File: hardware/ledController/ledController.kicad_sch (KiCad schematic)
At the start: 5 parts, among them IC1 PIC16F1769-I_ML, J1 Conn_01x06

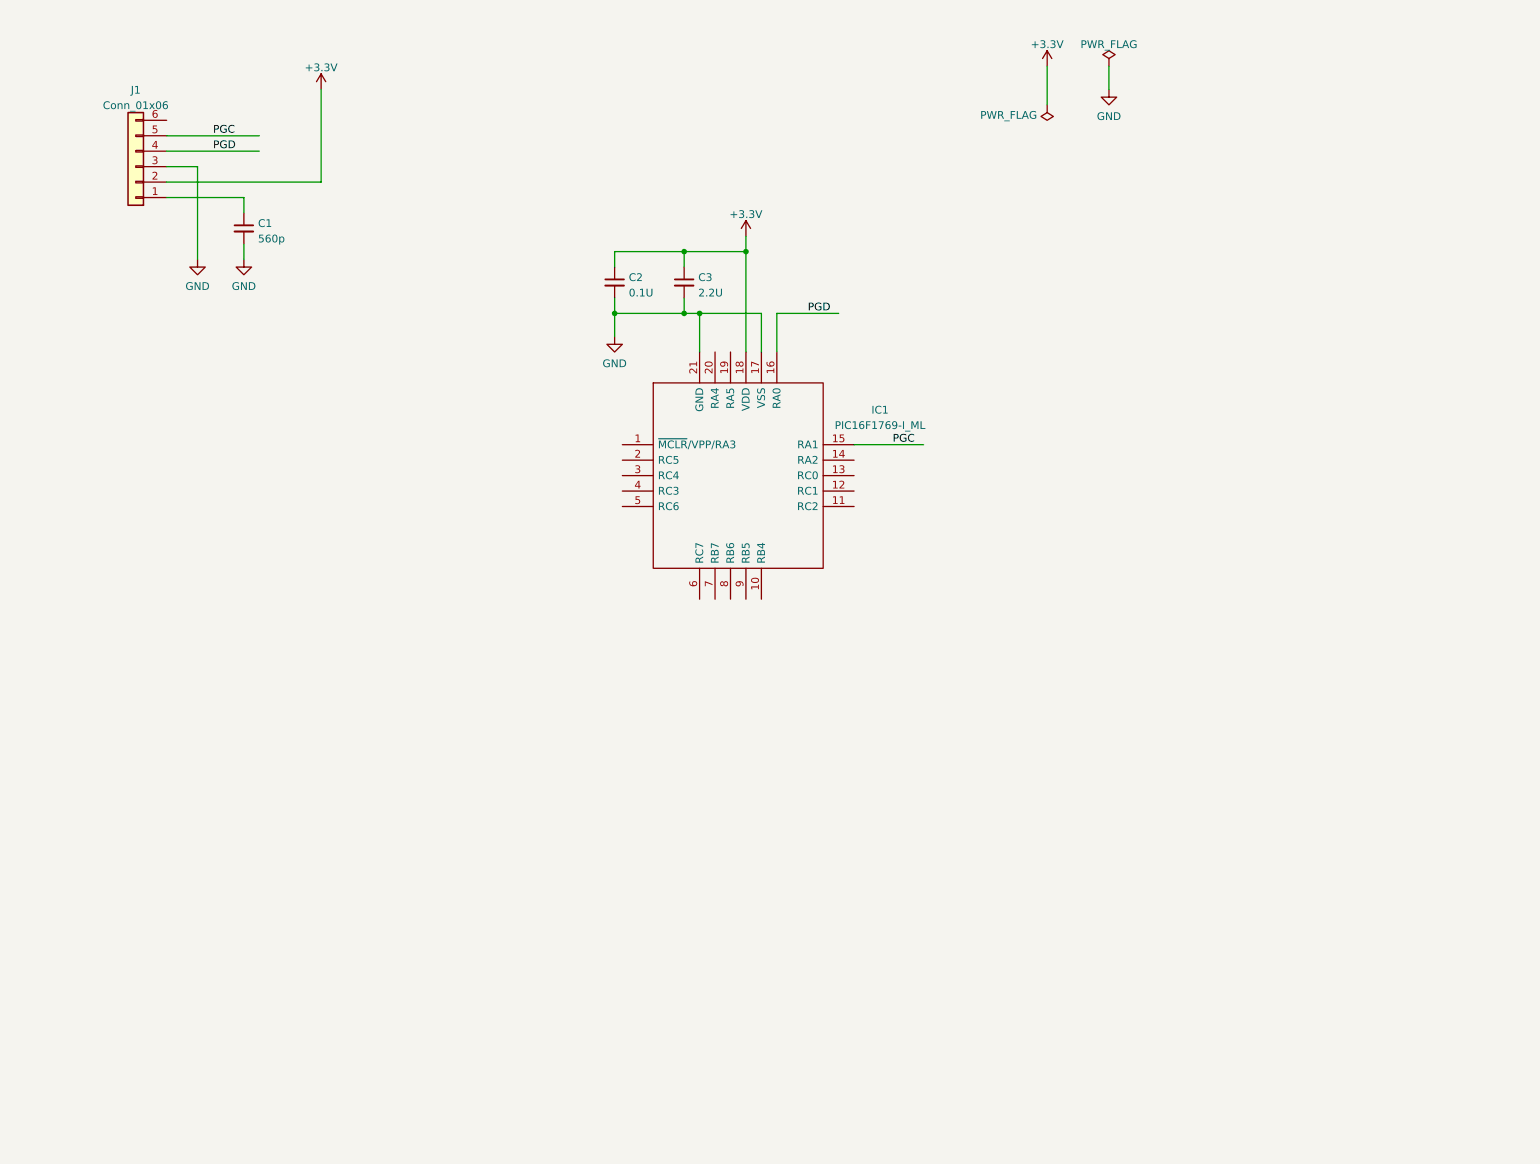
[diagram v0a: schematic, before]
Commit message: Incorporated the led driver to the main design
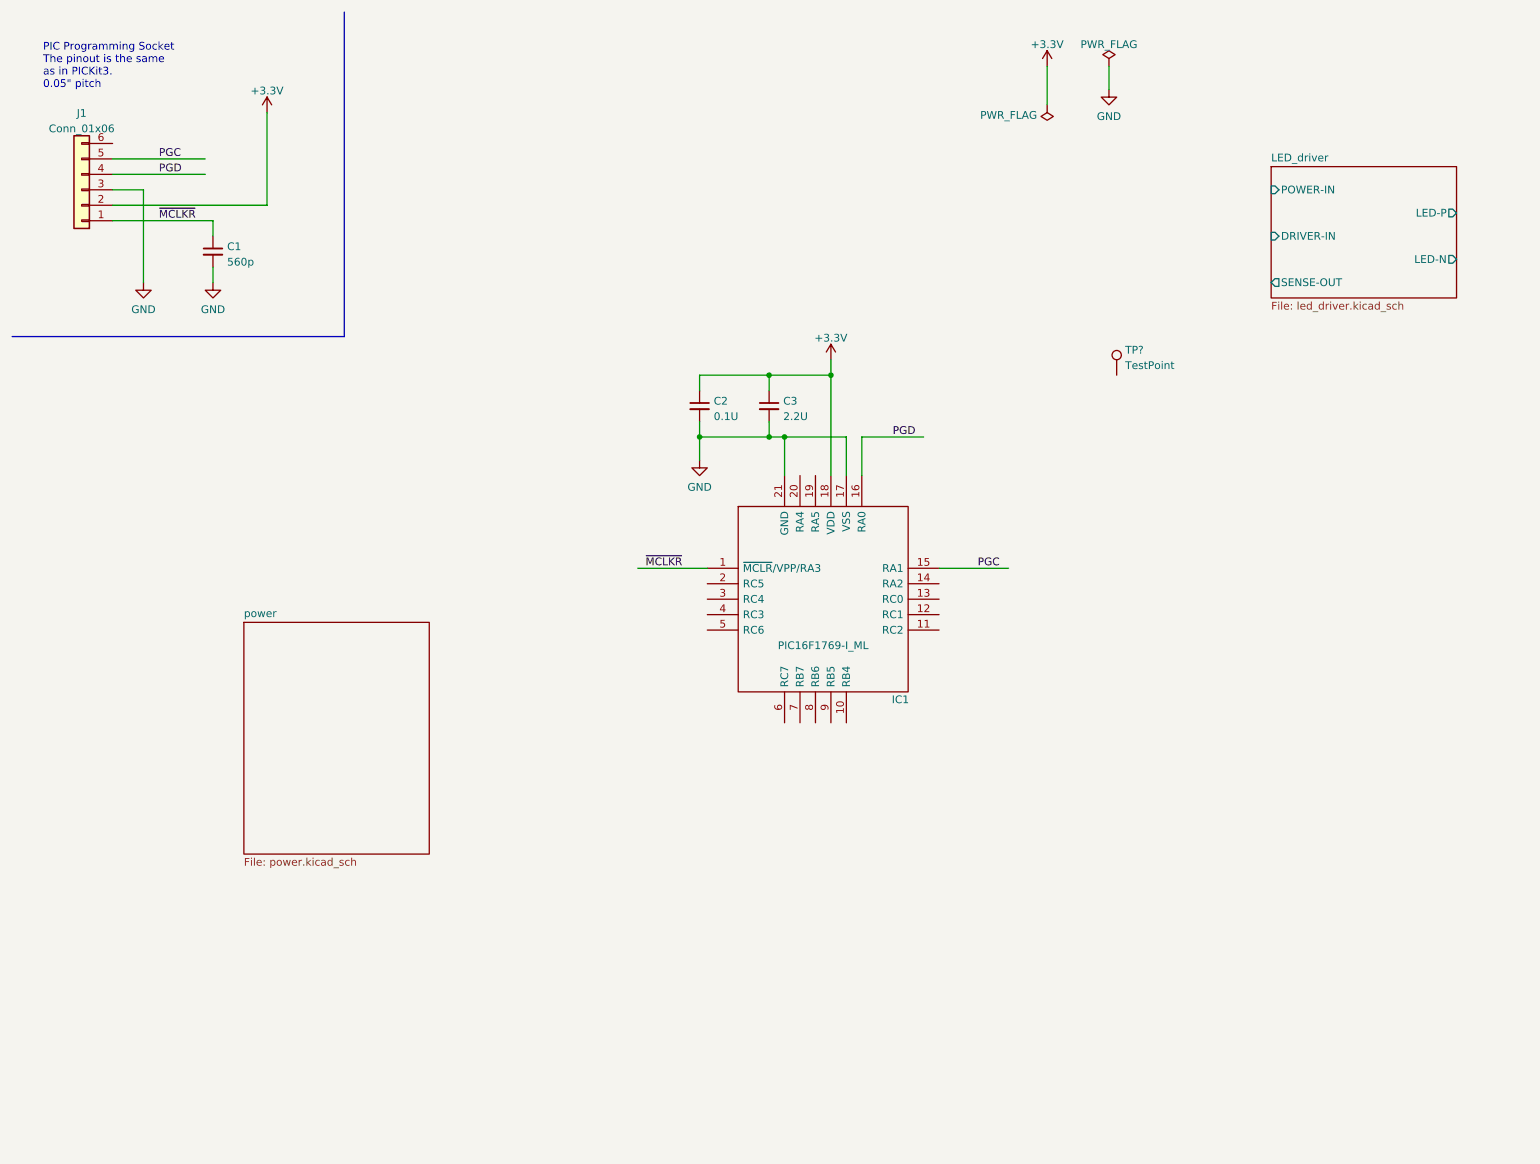
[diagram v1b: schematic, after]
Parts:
- added TP?: TestPoint, symbol Connector:TestPoint
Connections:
- net ~{MCLKR}: now reaches C1.1, J1.1 (Pin_1)
- net ~{MCLKR}: now also IC1.1 (~{MCLR}/VPP/RA3)
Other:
- added sheet LED_driver (led_driver.kicad_sch)
- added sheet power (power.kicad_sch)
- note added: "PIC Programming Socket The pinout is the same as in PICKit3. 0.05" pitch"
- moved on the sheet: C1, C2, C3, IC1, J1

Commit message: Added serial comm
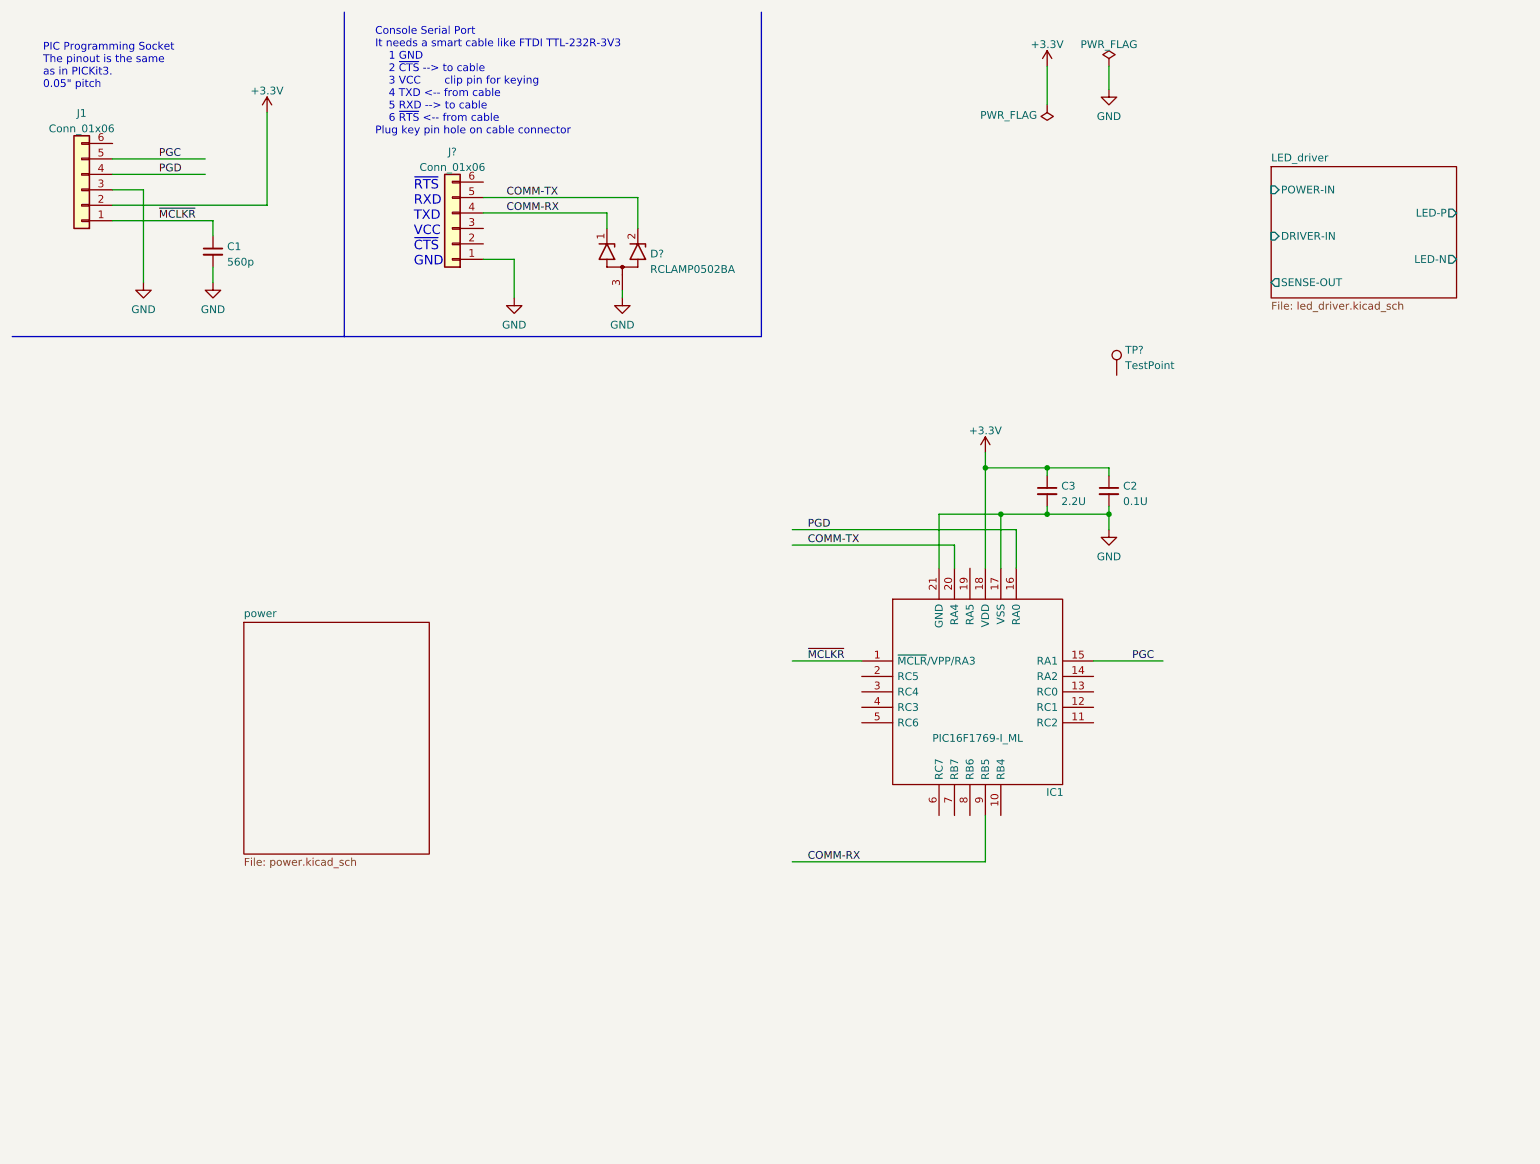
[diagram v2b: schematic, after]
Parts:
- added D?: RCLAMP0502BA, Package_TO_SOT_SMD:SOT-523, symbol Power_Protection:RCLAMP0502BA
- added J?: Conn_01x06, Connector_PinHeader_2.54mm:PinHeader_1x06_P2.54mm_Vertical, symbol Connector_Generic:Conn_01x06
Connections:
- net GND: now also D?.3 (A), J?.1 (Pin_1)
- net COMM-TX: now reaches IC1.20 (RA4)
- net COMM-TX: now also D?.2 (K2), J?.5 (Pin_5)
- net COMM-RX: now reaches IC1.9 (RB5)
- net COMM-RX: now also D?.1 (K1), J?.4 (Pin_4)
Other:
- note added: "Console Serial Port It needs a smart cable like FTDI TTL-232R-3V3 1 GND 2 ~{CTS} --> to cable 3 VCC clip pin for keying 4 TXD <-- from cable 5 RXD --> to cable 6 ~{RTS} <-- from cable Plug key pin hole on cable connector"
- note added: "~{RTS} RXD TXD VCC ~{CTS} GND"
- moved on the sheet: C2, C3, IC1

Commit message: Putting everything together
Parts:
- removed TP?: TestPoint, symbol Connector:TestPoint
- added C9: 4.7uF, Capacitor_SMD:C_0402_1005Metric_Pad0.74x0.62mm_HandSolder, symbol Device:C_Small
- added D1: B340, Diode_SMD:D_SMC, symbol Diode:B340
- added D3: LED_G, symbol Device:LED_Small
- added J2, J3: Screw_Terminal_01x02, symbol Connector:Screw_Terminal_01x02
- added R3: 200K, Resistor_SMD:R_0603_1608Metric_Pad0.98x0.95mm_HandSolder, symbol Device:R_Small_US
- added R4: 10K, Resistor_SMD:R_0603_1608Metric_Pad0.98x0.95mm_HandSolder, symbol Device:R_Small_US
- added R5: 2.4K, Resistor_SMD:R_0603_1608Metric_Pad0.98x0.95mm_HandSolder, symbol Device:R_Small_US
- gave numbers to parts that had none: 2
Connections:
- net GND: now also C9.2, J2.1 (Pin_1), R4.2, R5.2
- net LED_driver/LED-N: now also J3.2 (Pin_2)
- net LED_driver/LED-P: now also J3.1 (Pin_1)
- net OPA-FB: now reaches IC1.10 (RB4)
- net OPA-OUT: now reaches IC1.11 (RC2)
- net V_{IN}: now reaches IC1.4 (RC3)
- net V_{IN}: now also R3.2, R4.1
- net at IC1.6 (RC7): now also D3.2 (A)
- new net: D1.2 (A), J2.2 (Pin_2)
- new net: D3.1 (K), R5.1
- new net VDC: C9.1, D1.1 (K), R3.1
- no-connect marks 0 -> 13
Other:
- sheet power: file power.kicad_sch -> power_3p3V.kicad_sch
- sheet power ports: added V_{IN}, V_{OUT}; removed none
- note added: "Console Serial Port"
- note added: "It needs a smart cable like FTDI TTL-232R-3V3 1 GND 2 ~{CTS} --> to cable 3 VCC clip pin for keying 4 TXD <-- from cable 5 RXD --> to cable 6 ~{RTS} <-- from cable Plug key pin hole on cable connector"
- note added: "LED Driver Block"
- note added: "PIC Programming Socket"
- note added: "Power Supply Block"
- note added: "The pinout is the same as in PICKit3. 0.05" pitch"
- note added: "When VDC = 12V, V_{IN} = 0.57V When VDC = 50V, V_{IN} = 2.38V"
- note removed: "Console Serial Port It needs a smart cable like FTDI TTL-232R-3V3 1 GND 2 ~{CTS} --> to cable 3 VCC clip pin for keying 4 TXD <-- from cable 5 RXD --> to cable 6 ~{RTS} <-- from cable Plug key pin hole on cable connector"
- note removed: "PIC Programming Socket The pinout is the same as in PICKit3. 0.05" pitch"
- title: (none) -> Lantern
- moved on the sheet: C2, C3, IC1

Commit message: First attempt of schematic to PCB
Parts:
- removed C9: 4.7uF, Capacitor_SMD:C_0402_1005Metric_Pad0.74x0.62mm_HandSolder, symbol Device:C_Small
- added J5: Conn_01x03, molex-footprints:353620350, symbol Connector_Generic:Conn_01x03
- D3: footprint (none) -> LED_SMD:LED_0805_2012Metric_Pad1.15x1.40mm_HandSolder
- J2, J3: footprint (none) -> TerminalBlock:TerminalBlock_Altech_AK300-2_P5.00mm
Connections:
- net +3.3V: now also J5.3 (Pin_3)
- net GND: now also J5.1 (Pin_1)
- new net PIR-OUT: J5.2 (Pin_2)
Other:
- sheet power: file power_3p3V.kicad_sch -> power_module.kicad_sch
- note added: "Designed to work with Grove - mini PIR motion sensor https://media.digikey.com/pdf/Data%20Sheets/Seeed%20Technology/101020353_Web.pdf"
- note added: "PIR Proximity Sensor Connector"
